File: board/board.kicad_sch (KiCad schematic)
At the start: 29 parts, among them J1 port attiny, J10 BMS Bat +, J11 BMS Bat gnd, J12 BMS out -, J13 BMS in +5v, J14 BMS in gnd, J15_C189893 BMS led charge ok, J16 Mp3 D1 led marche ok, J17_C189893 Haut parleur, J18_C189893 Batterie + et -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

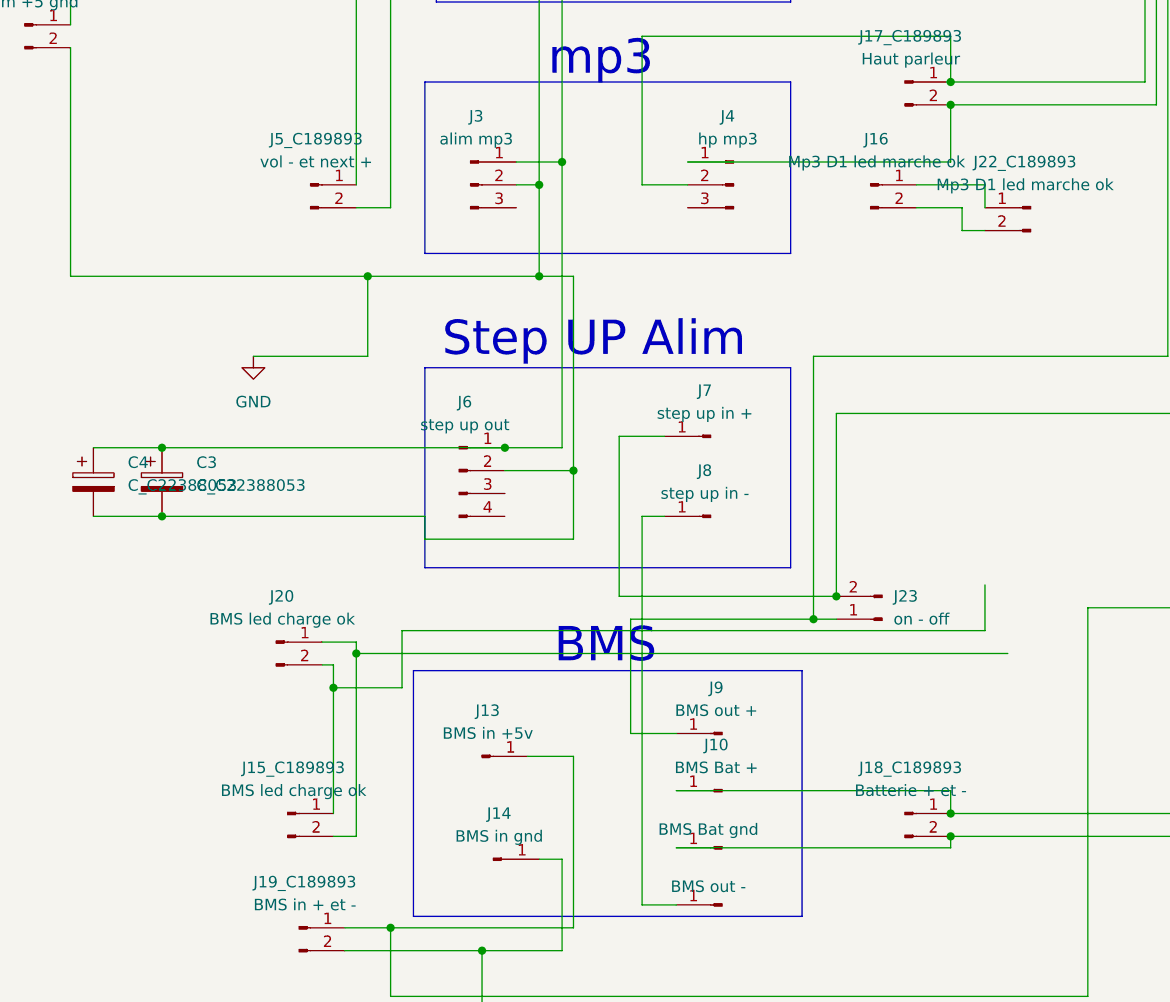
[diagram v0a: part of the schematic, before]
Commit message: correction sens pin vue 3D
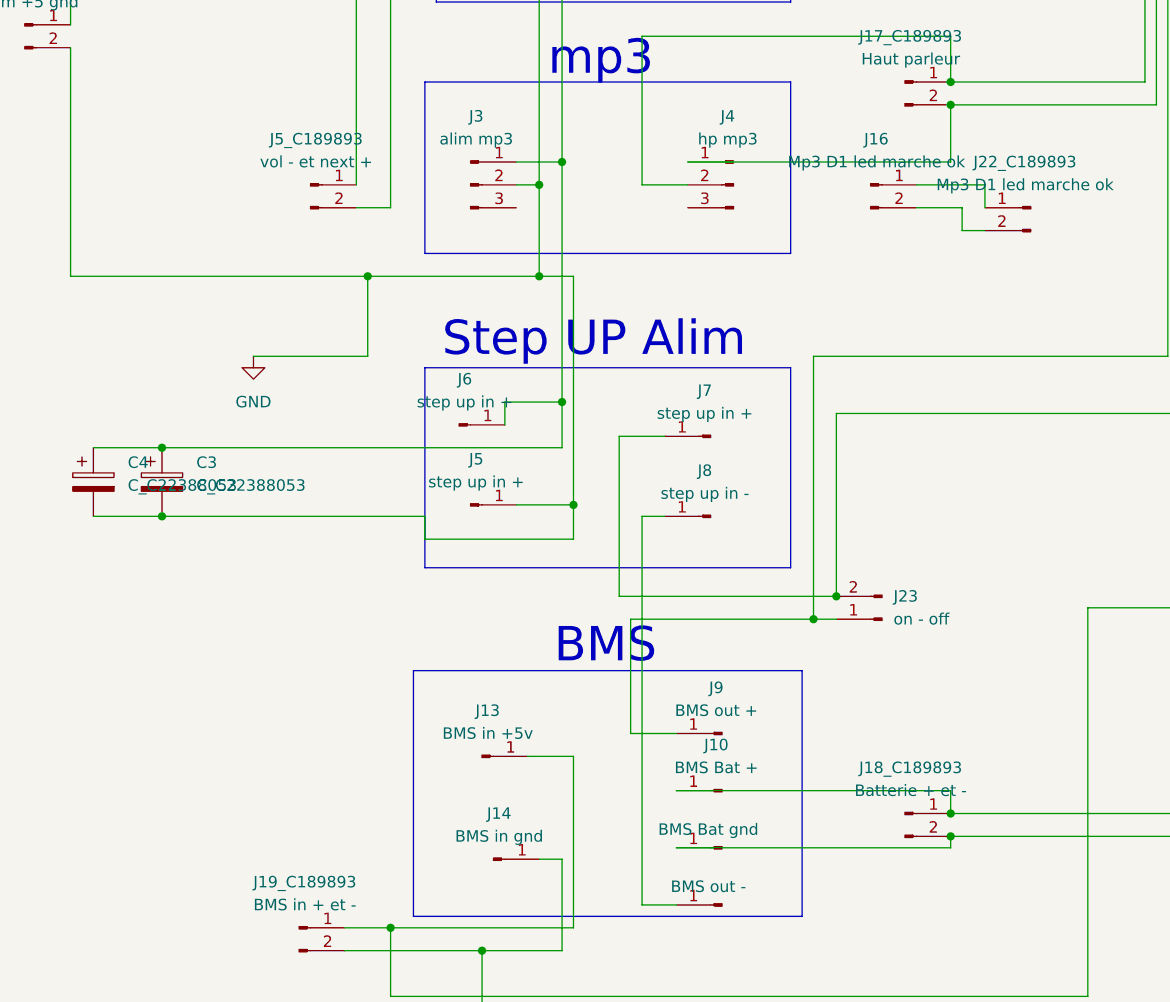
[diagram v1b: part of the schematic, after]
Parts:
- removed J15_C189893: BMS led charge ok, Connector_JST:JST_GH_BM02B-GHS-TBT_1x02-1MP_P1.25mm_Vertical, symbol Connector:Conn_01x02_Pin
- removed J20: BMS led charge ok, Connector_PinSocket_2.54mm:PinSocket_1x02_P2.54mm_Vertical, symbol Connector:Conn_01x02_Pin
- removed J6: step up out, Library:PinHeader_1x04_P2.54mm_Vertical-mp3, symbol Connector:Conn_01x04_Pin
- added J5, J6: step up in +, Connector_PinHeader_2.54mm:PinHeader_1x01_P2.54mm_Vertical, symbol Connector:Conn_01x01_Pin
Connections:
- net GND: now also J5.1 (Pin_1)
- net VCC: now also J6.1 (Pin_1)

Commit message: ajout serigraphie pour faciliter le montage
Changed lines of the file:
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@@
 	(wire
 		(pts
-			(xy 201.93 97.79) (xy 250.19 97.79)
-		)
-		(stroke
-			(width 0)
-			(type default)
-		)
-	)
-	(wire
-		(pts
-			(xy 209.55 59.69) (xy 209.55 90.17)
+			(xy 165.1 78.74) (xy 165.1 90.17)
 		)
 		(stroke
@@
 	(wire
 		(pts
-			(xy 139.7 160.02) (xy 187.96 160.02)
+			(xy 139.7 160.02) (xy 157.48 160.02)
 		)
 		(stroke
@@
 	(wire
 		(pts
-			(xy 165.1 132.08) (xy 168.91 132.08)
+			(xy 162.56 133.35) (xy 212.09 133.35)
 		)
 		(stroke
@@
 	(wire
 		(pts
-			(xy 187.96 139.7) (xy 229.87 139.7)
+			(xy 157.48 139.7) (xy 229.87 139.7)
 		)
 		(stroke
@@
 	(wire
 		(pts
-			(xy 124.46 109.22) (xy 163.83 109.22)
-		)
-		(stroke
-			(width 0)
-			(type default)
-		)
-	)
-	(wire
-		(pts
-			(xy 212.09 134.62) (xy 212.09 100.33)
+			(xy 124.46 109.22) (xy 165.1 109.22)
+		)
+		(stroke
+			(width 0)
+			(type default)
+		)
+	)
+	(wire
+		(pts
+			(xy 212.09 133.35) (xy 212.09 100.33)
 		)
 		(stroke
@@
 	(wire
 		(pts
-			(xy 168.91 134.62) (xy 212.09 134.62)
-		)
-		(stroke
-			(width 0)
-			(type default)
-		)
-	)
-	(wire
-		(pts
 			(xy 97.79 153.67) (xy 92.71 153.67)
 		)
@@
 	(wire
 		(pts
-			(xy 163.83 64.77) (xy 204.47 64.77)
+			(xy 160.02 162.56) (xy 160.02 143.51)
+		)
+		(stroke
+			(width 0)
+			(type default)
+		)
+	)
+	(wire
+		(pts
+			(xy 165.1 95.25) (xy 248.92 95.25)
 		)
 		(stroke
@@
 	(wire
 		(pts
-			(xy 127 115.57) (xy 166.37 115.57)
+			(xy 127 115.57) (xy 167.64 115.57)
 		)
 		(stroke
@@
 	(wire
 		(pts
-			(xy 209.55 90.17) (xy 246.38 90.17)
+			(xy 165.1 90.17) (xy 246.38 90.17)
 		)
 		(stroke
@@
 	(wire
 		(pts
-			(xy 191.77 142.24) (xy 233.68 142.24)
+			(xy 160.02 143.51) (xy 233.68 143.51)
 		)
 		(stroke
@@
 	(wire
 		(pts
-			(xy 139.7 162.56) (xy 191.77 162.56)
-		)
-		(stroke
-			(width 0)
-			(type default)
-		)
-	)
-	(wire
-		(pts
 			(xy 41.91 33.02) (xy 41.91 72.39)
 		)
@@
 	(wire
 		(pts
-			(xy 139.7 78.74) (xy 161.29 78.74)
-		)
-		(stroke
-			(width 0)
-			(type default)
-		)
-	)
-	(wire
-		(pts
-			(xy 134.62 64.77) (xy 160.02 64.77)
+			(xy 139.7 78.74) (xy 165.1 78.74)
+		)
+		(stroke
+			(width 0)
+			(type default)
+		)
+	)
+	(wire
+		(pts
+			(xy 134.62 64.77) (xy 208.28 64.77)
 		)
 		(stroke
@@
 	(wire
 		(pts
-			(xy 166.37 67.31) (xy 201.93 67.31)
+			(xy 167.64 97.79) (xy 250.19 97.79)
 		)
 		(stroke
@@
 	(wire
 		(pts
-			(xy 161.29 78.74) (xy 161.29 59.69)
-		)
-		(stroke
-			(width 0)
-			(type default)
-		)
-	)
-	(wire
-		(pts
-			(xy 204.47 95.25) (xy 248.92 95.25)
-		)
-		(stroke
-			(width 0)
-			(type default)
-		)
-	)
-	(wire
-		(pts
 			(xy 212.09 100.33) (xy 251.46 100.33)
 		)
@@
 	(wire
 		(pts
-			(xy 212.09 87.63) (xy 245.11 87.63)
+			(xy 208.28 87.63) (xy 245.11 87.63)
 		)
 		(stroke
@@
 	(wire
 		(pts
-			(xy 165.1 186.69) (xy 165.1 132.08)
+			(xy 162.56 177.8) (xy 162.56 133.35)
 		)
 		(stroke
@@
 	(wire
 		(pts
-			(xy 87.63 175.26) (xy 87.63 186.69)
+			(xy 87.63 175.26) (xy 87.63 177.8)
 		)
 		(stroke
@@
 	(wire
 		(pts
-			(xy 207.01 62.23) (xy 207.01 92.71)
-		)
-		(stroke
-			(width 0)
-			(type default)
-		)
-	)
-	(wire
-		(pts
 			(xy 77.47 180.34) (xy 154.94 180.34)
 		)
@@
 	(wire
 		(pts
-			(xy 191.77 162.56) (xy 191.77 142.24)
-		)
-		(stroke
-			(width 0)
-			(type default)
-		)
-	)
-	(wire
-		(pts
 			(xy 44.45 119.38) (xy 52.07 119.38)
 		)
@@
 	(wire
 		(pts
-			(xy 166.37 115.57) (xy 166.37 67.31)
+			(xy 167.64 115.57) (xy 167.64 97.79)
 		)
 		(stroke
@@
 	(wire
 		(pts
-			(xy 214.63 54.61) (xy 214.63 85.09)
-		)
-		(stroke
-			(width 0)
-			(type default)
-		)
-	)
-	(wire
-		(pts
-			(xy 158.75 63.5) (xy 158.75 54.61)
+			(xy 160.02 162.56) (xy 139.7 162.56)
+		)
+		(stroke
+			(width 0)
+			(type default)
+		)
+	)
+	(wire
+		(pts
+			(xy 214.63 63.5) (xy 214.63 85.09)
 		)
 		(stroke
@@
 	(wire
 		(pts
-			(xy 201.93 67.31) (xy 201.93 97.79)
-		)
-		(stroke
-			(width 0)
-			(type default)
-		)
-	)
-	(wire
-		(pts
 			(xy 93.98 100.33) (xy 97.79 100.33)
 		)
@@
 	(wire
 		(pts
-			(xy 212.09 57.15) (xy 212.09 87.63)
+			(xy 208.28 64.77) (xy 208.28 87.63)
 		)
 		(stroke
@@
 	(wire
 		(pts
-			(xy 87.63 186.69) (xy 165.1 186.69)
+			(xy 87.63 177.8) (xy 162.56 177.8)
 		)
 		(stroke
@@
 	(wire
 		(pts
-			(xy 162.56 81.28) (xy 162.56 62.23)
+			(xy 162.56 81.28) (xy 162.56 92.71)
 		)
 		(stroke
@@
 	(wire
 		(pts
-			(xy 187.96 160.02) (xy 187.96 139.7)
+			(xy 157.48 160.02) (xy 157.48 139.7)
 		)
 		(stroke
@@
 	(wire
 		(pts
-			(xy 168.91 132.08) (xy 168.91 134.62)
-		)
-		(stroke
-			(width 0)
-			(type default)
-		)
-	)
-	(wire
-		(pts
-			(xy 158.75 54.61) (xy 214.63 54.61)
-		)
-		(stroke
-			(width 0)
-			(type default)
-		)
-	)
-	(wire
-		(pts
 			(xy 243.84 80.01) (xy 261.62 80.01)
 		)
@@
 	(wire
 		(pts
-			(xy 160.02 64.77) (xy 160.02 57.15)
-		)
-		(stroke
-			(width 0)
-			(type default)
-		)
-	)
-	(wire
-		(pts
 			(xy 246.38 90.17) (xy 246.38 85.09)
 		)
@@
 	(wire
 		(pts
-			(xy 134.62 63.5) (xy 158.75 63.5)
+			(xy 134.62 63.5) (xy 214.63 63.5)
 		)
 		(stroke
@@
 	(wire
 		(pts
-			(xy 161.29 59.69) (xy 209.55 59.69)
-		)
-		(stroke
-			(width 0)
-			(type default)
-		)
-	)
-	(wire
-		(pts
 			(xy 105.41 73.66) (xy 139.7 73.66)
 		)
@@
 	(wire
 		(pts
-			(xy 233.68 142.24) (xy 233.68 107.95)
-		)
-		(stroke
-			(width 0)
-			(type default)
-		)
-	)
-	(wire
-		(pts
-			(xy 160.02 57.15) (xy 212.09 57.15)
+			(xy 233.68 143.51) (xy 233.68 107.95)
 		)
 		(stroke
@@
 	(wire
 		(pts
-			(xy 162.56 62.23) (xy 207.01 62.23)
+			(xy 162.56 92.71) (xy 247.65 92.71)
 		)
 		(stroke
@@
 	(wire
 		(pts
-			(xy 204.47 64.77) (xy 204.47 95.25)
-		)
-		(stroke
-			(width 0)
-			(type default)
-		)
-	)
-	(wire
-		(pts
 			(xy 102.87 135.89) (xy 127 135.89)
 		)
@@
 	(wire
 		(pts
-			(xy 163.83 109.22) (xy 163.83 64.77)
+			(xy 165.1 109.22) (xy 165.1 95.25)
 		)
 		(stroke
@@
 		)
 		(stroke
-			(width 0)
-			(type default)
-		)
-	)
-	(wire
-		(pts
-			(xy 207.01 92.71) (xy 247.65 92.71)
-		)
-		(stroke

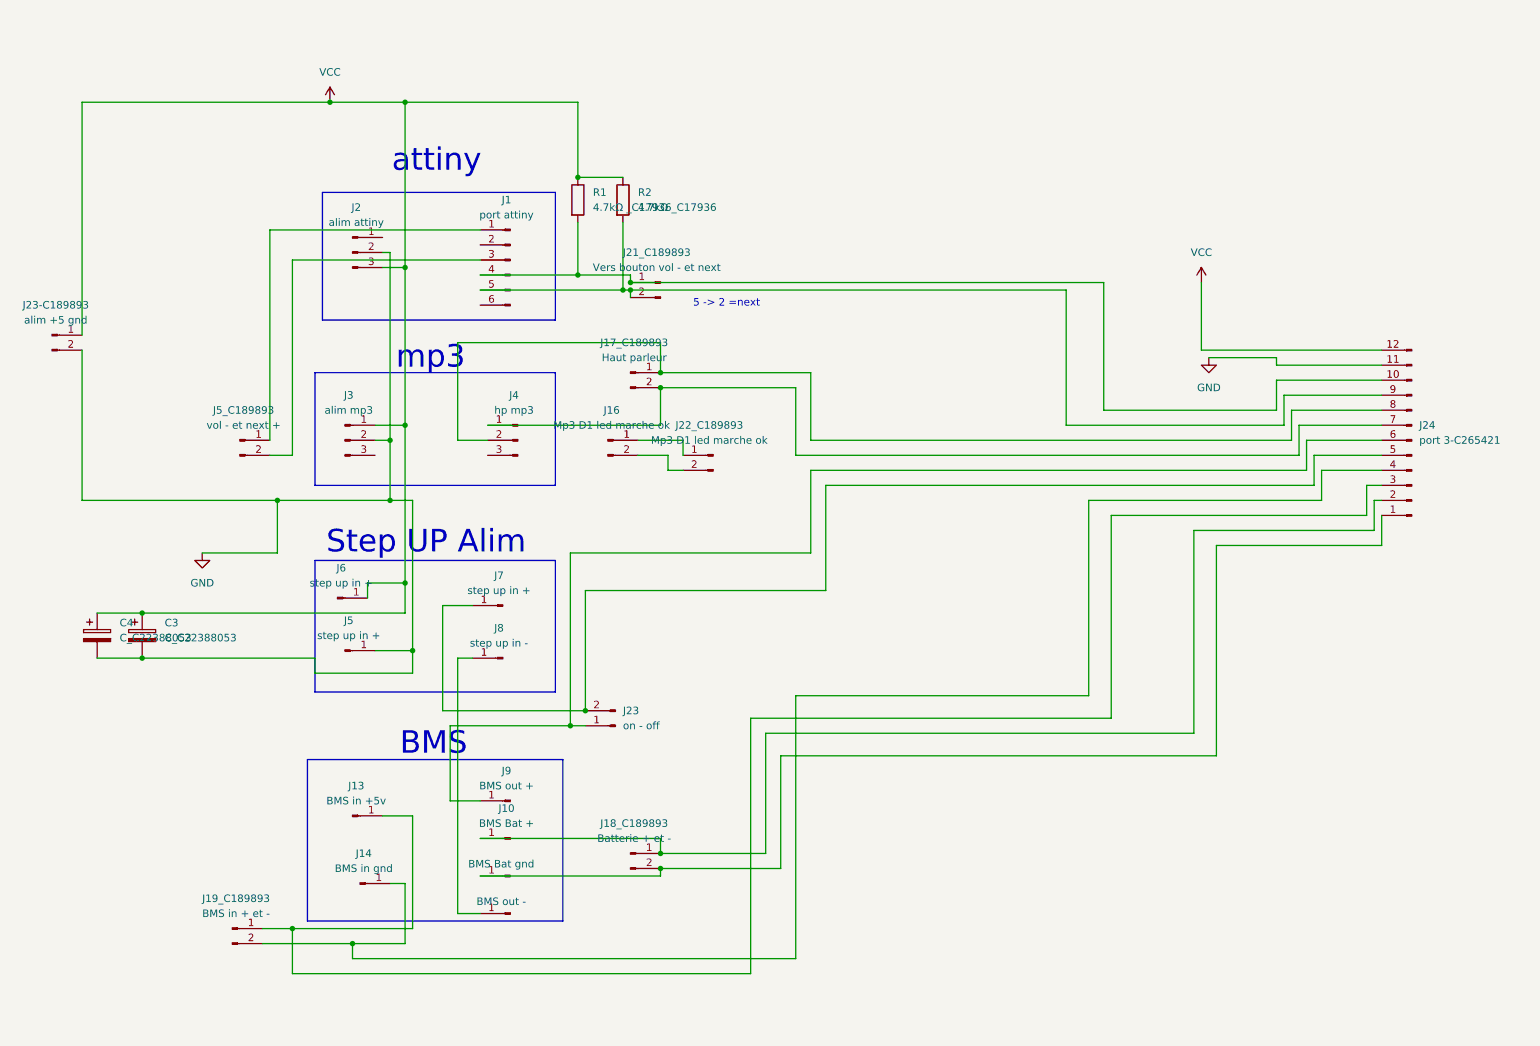
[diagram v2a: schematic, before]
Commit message: ajout connecteur programmation tiny85
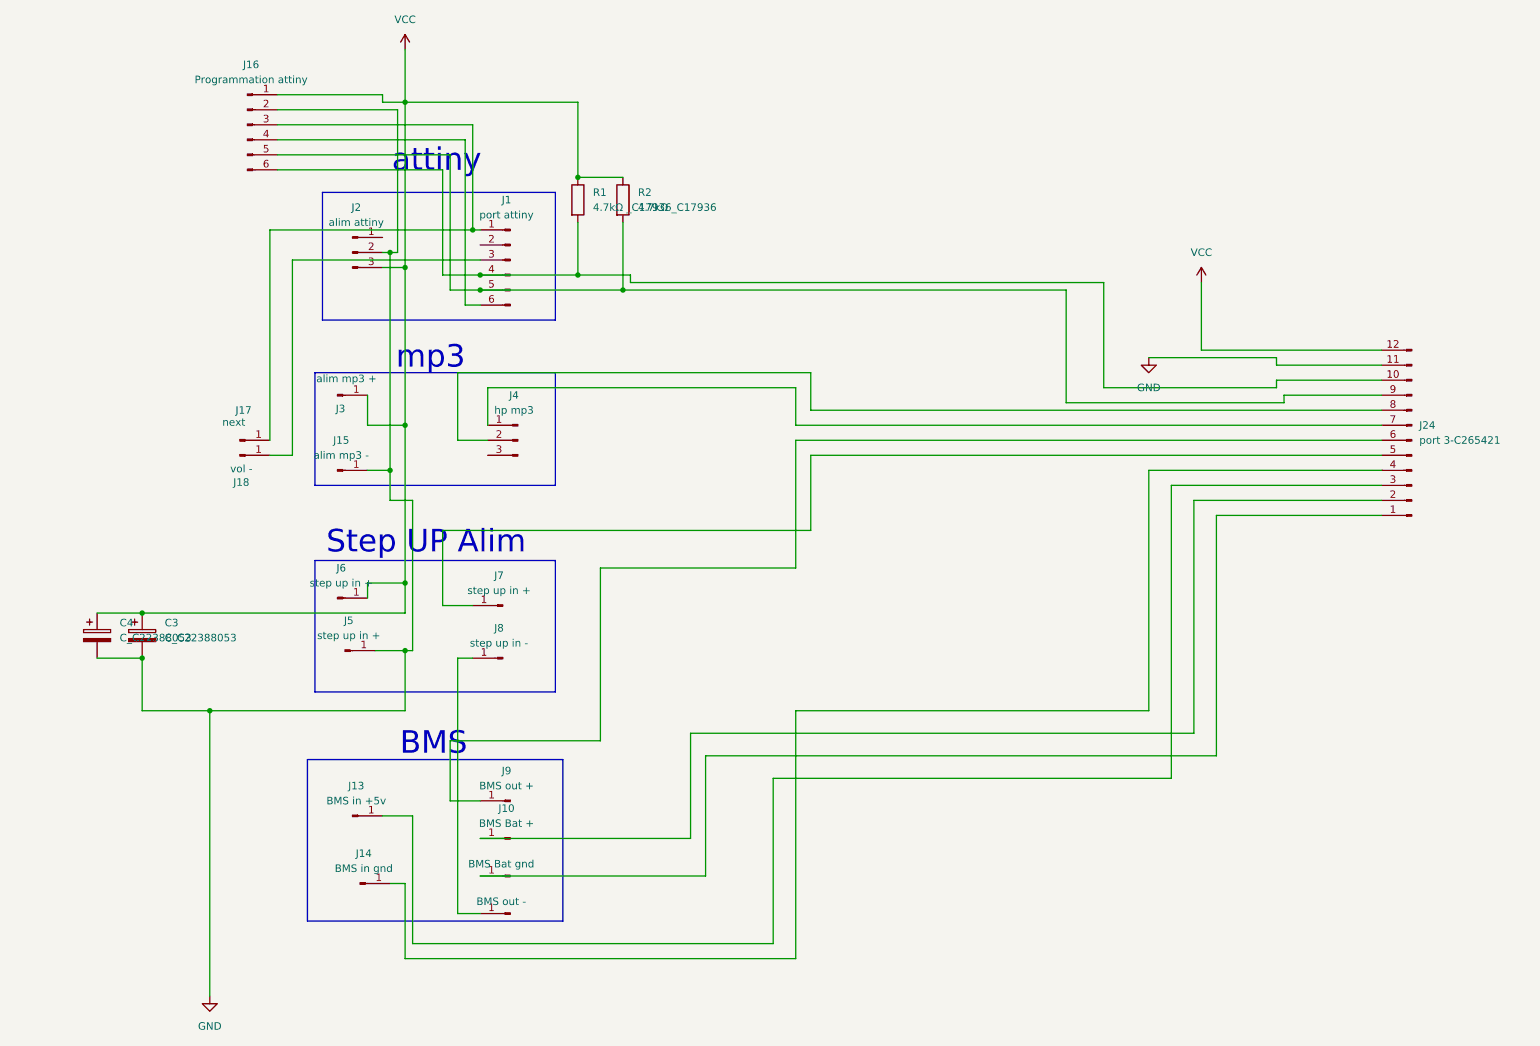
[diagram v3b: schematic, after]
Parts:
- removed J16: Mp3 D1 led marche ok, Connector_PinHeader_2.54mm:PinHeader_1x02_P2.54mm_Vertical, symbol Connector:Conn_01x02_Pin
- removed J17_C189893: Haut parleur, Connector_JST:JST_GH_BM02B-GHS-TBT_1x02-1MP_P1.25mm_Vertical, symbol Connector:Conn_01x02_Pin
- removed J18_C189893: Batterie + et -, Connector_JST:JST_GH_BM02B-GHS-TBT_1x02-1MP_P1.25mm_Vertical, symbol Connector:Conn_01x02_Pin
- removed J19_C189893: BMS in + et -, Connector_JST:JST_GH_BM02B-GHS-TBT_1x02-1MP_P1.25mm_Vertical, symbol Connector:Conn_01x02_Pin
- removed J21_C189893: Vers bouton vol - et next, Connector_JST:JST_GH_BM02B-GHS-TBT_1x02-1MP_P1.25mm_Vertical, symbol Connector:Conn_01x02_Pin
- removed J22_C189893: Mp3 D1 led marche ok, Connector_JST:JST_GH_BM02B-GHS-TBT_1x02-1MP_P1.25mm_Vertical, symbol Connector:Conn_01x02_Pin
- removed J23: on - off, Connector_JST:JST_GH_BM02B-GHS-TBT_1x02-1MP_P1.25mm_Vertical, symbol Connector:Conn_01x02_Pin
- removed J23-C189893: alim +5 gnd, Connector_JST:JST_GH_BM02B-GHS-TBT_1x02-1MP_P1.25mm_Vertical, symbol Connector:Conn_01x02_Pin
- removed J3: alim mp3, Library:PinHeader_1x03_P2.54mm_Vertical-mp3, symbol Connector:Conn_01x03_Pin
- removed J5_C189893: vol - et next +, Connector_PinHeader_2.54mm:PinHeader_1x02_P2.54mm_Vertical, symbol Connector:Conn_01x02_Pin
- added J15: alim mp3 -, Connector_PinHeader_2.54mm:PinHeader_1x01_P2.54mm_Vertical, symbol Connector:Conn_01x01_Pin
- added J16: Programmation attiny, Connector_JST:JST_PH_B6B-PH-K_1x06_P2.00mm_Vertical, symbol Connector:Conn_01x06_Pin
- added J17: next, Connector_PinHeader_2.54mm:PinHeader_1x01_P2.54mm_Vertical, symbol Connector:Conn_01x01_Pin
- added J18: vol -, Connector_PinHeader_2.54mm:PinHeader_1x01_P2.54mm_Vertical, symbol Connector:Conn_01x01_Pin
- added J3: alim mp3 +, Connector_PinHeader_2.54mm:PinHeader_1x01_P2.54mm_Vertical, symbol Connector:Conn_01x01_Pin
- J24: footprint Connector_JST:JST_GH_SM12B-GHS-TB_1x12-1MP_P1.25mm_Horizontal -> Connector_JST:JST_GH_BM12B-GHS-TBT_1x12-1MP_P1.25mm_Vertical
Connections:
- net GND: now also J15.1 (Pin_1), J16.2 (Pin_2)
- net VCC: now also J16.1 (Pin_1), J3.1 (Pin_1)
- net at J1.1 (Pin_1): now also J16.3 (Pin_3), J17.1 (Pin_1)
- net at J1.3 (Pin_3): now also J18.1 (Pin_1)
- net at J1.4 (Pin_4), J24.10 (Pin_10), R1.2: now also J16.6 (Pin_6)
- net at J1.5 (Pin_5), J24.9 (Pin_9), R2.2: now also J16.5 (Pin_5)
- net at J1.6 (Pin_6): now also J16.4 (Pin_4)
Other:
- note removed: "5 -> 2 =next"
